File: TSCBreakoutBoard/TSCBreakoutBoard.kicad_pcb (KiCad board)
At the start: 2 copper layers, 26 x 31 mm, 7 parts, among them J1 CH 1, J2 CH2, J3 CH 3, J4 CH 4, J5 RJ45

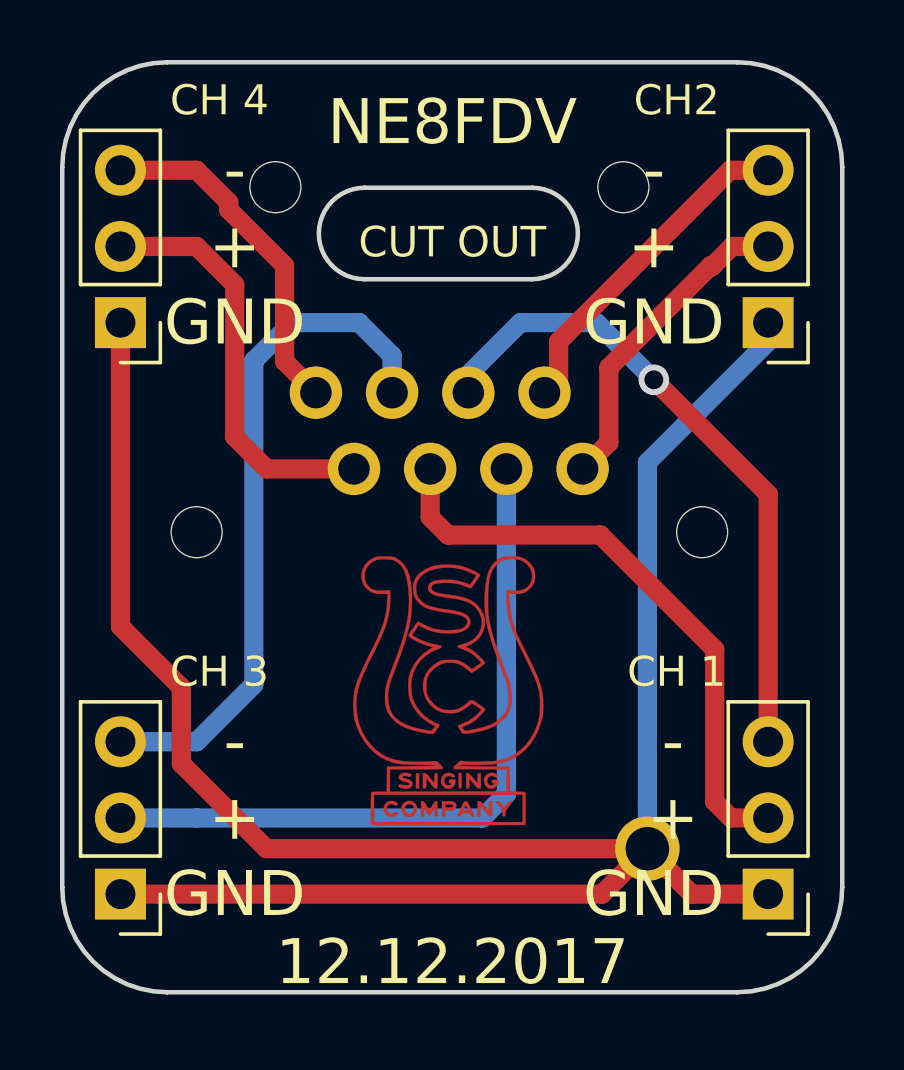
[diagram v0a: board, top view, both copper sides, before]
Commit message: remove logo & date
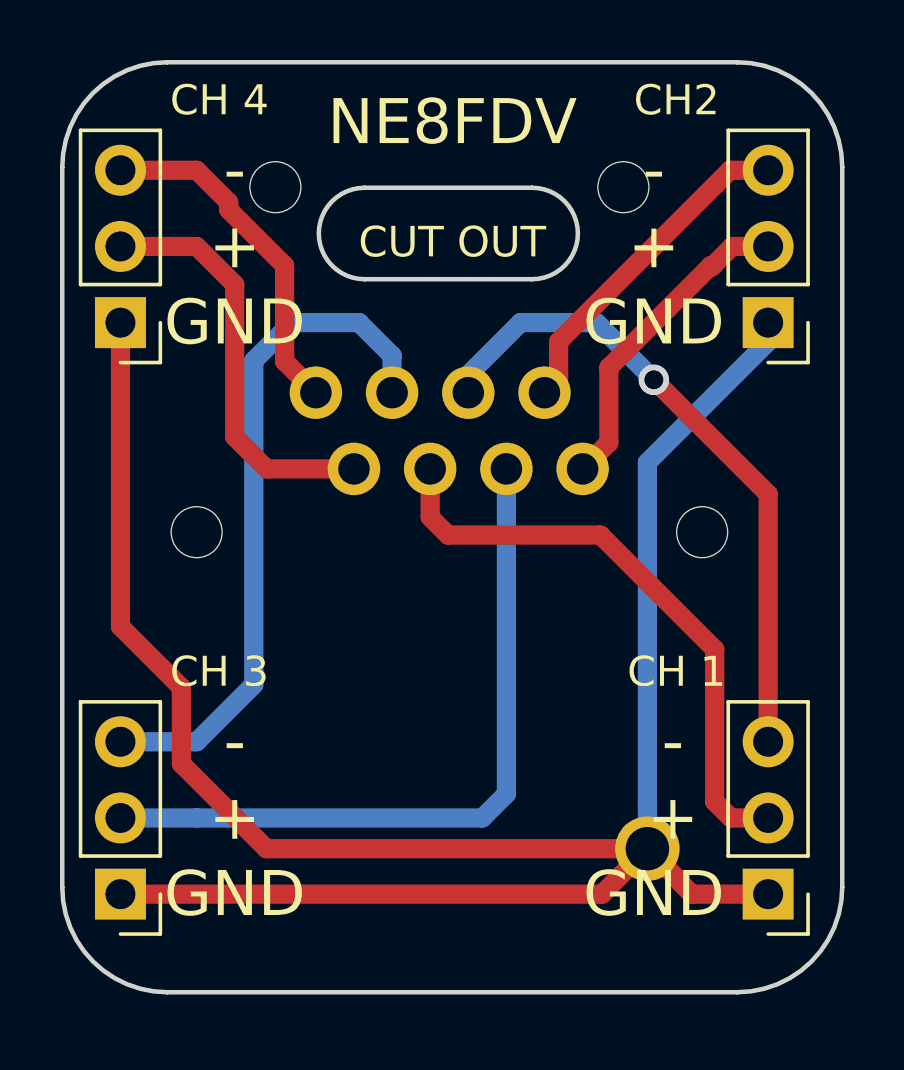
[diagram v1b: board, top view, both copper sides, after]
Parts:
- removed G***: LOGO, logo:TSC
- removed G***: LOGO, logo:TSCMask
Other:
- board text removed: "12.12.2017"
